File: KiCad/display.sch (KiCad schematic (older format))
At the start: 72 parts, among them IC11 SN74LV1T125DBVR, IC6 PCA9517ADP, J1 46756-1001, J2 2129320-3, T1 BSS138APW

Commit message: TLV70018DCKT -> TPS7A0518PDBVT
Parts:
- U? (x3): footprint jetson-nano-baseboard-footprints:TPD4E05U06QDQARQ1 -> antmicro-footprints:TPD4E05U06QDQARQ1; symbol jetson-nano-baseboard:TPD4E05U06QDQARQ1 -> antmicroTVSDiodes:TPD4E05U06QDQARQ1
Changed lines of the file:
@@
 Connection ~ 4025 4600
 $Comp
-L jetson-nano-baseboard:TPD4E05U06QDQARQ1 U?
+L antmicroTVSDiodes:TPD4E05U06QDQARQ1 U?
 U 1 1 61B4F31F
 P 14275 7150
 F 0 "U?" V 14301 7478 50  0000 L CNN
 F 1 "TPD4E05U06QDQARQ1" H 14325 6750 50  0001 L CNN
-F 2 "jetson-nano-baseboard-footprints:TPD4E05U06QDQARQ1" H 14325 7600 50  0001 L CNN
+F 2 "antmicro-footprints:TPD4E05U06QDQARQ1" H 14325 7600 50  0001 L CNN
 F 3 "http://www.ti.com/general/docs/lit/getliterature.tsp?genericPartNumber=TPD4E001&fileType=pdf" H 14275 7550 50  0001 L CNN
 F 4 "Texas Instruments" V 14650 6850 50  0000 L CNN "Manufacturer"
@@
 $EndComp
 $Comp
-L jetson-nano-baseboard:TPD4E05U06QDQARQ1 U?
+L antmicroTVSDiodes:TPD4E05U06QDQARQ1 U?
 U 1 1 61B58F0C
 P 13825 9275
 F 0 "U?" V 13900 9600 50  0000 L CNN
 F 1 "TPD4E05U06QDQARQ1" H 13875 8875 50  0001 L CNN
-F 2 "jetson-nano-baseboard-footprints:TPD4E05U06QDQARQ1" H 13875 9725 50  0001 L CNN
+F 2 "antmicro-footprints:TPD4E05U06QDQARQ1" H 13875 9725 50  0001 L CNN
 F 3 "http://www.ti.com/general/docs/lit/getliterature.tsp?genericPartNumber=TPD4E001&fileType=pdf" H 13825 9675 50  0001 L CNN
 F 4 "Texas Instruments" V 14200 8975 50  0000 L CNN "Manufacturer"
@@
 Connection ~ 10550 10025
 $Comp
-L jetson-nano-baseboard:TPD4E05U06QDQARQ1 U?
+L antmicroTVSDiodes:TPD4E05U06QDQARQ1 U?
 U 1 1 61E47ECC
 P 10650 10450
 F 0 "U?" V 10676 10778 50  0000 L CNN
 F 1 "TPD4E05U06QDQARQ1" H 10700 10050 50  0001 L CNN
-F 2 "jetson-nano-baseboard-footprints:TPD4E05U06QDQARQ1" H 10700 10900 50  0001 L CNN
+F 2 "antmicro-footprints:TPD4E05U06QDQARQ1" H 10700 10900 50  0001 L CNN
 F 3 "http://www.ti.com/general/docs/lit/getliterature.tsp?genericPartNumber=TPD4E001&fileType=pdf" H 10650 10850 50  0001 L CNN
 F 4 "Texas Instruments" V 11025 10150 50  0000 L CNN "Manufacturer"

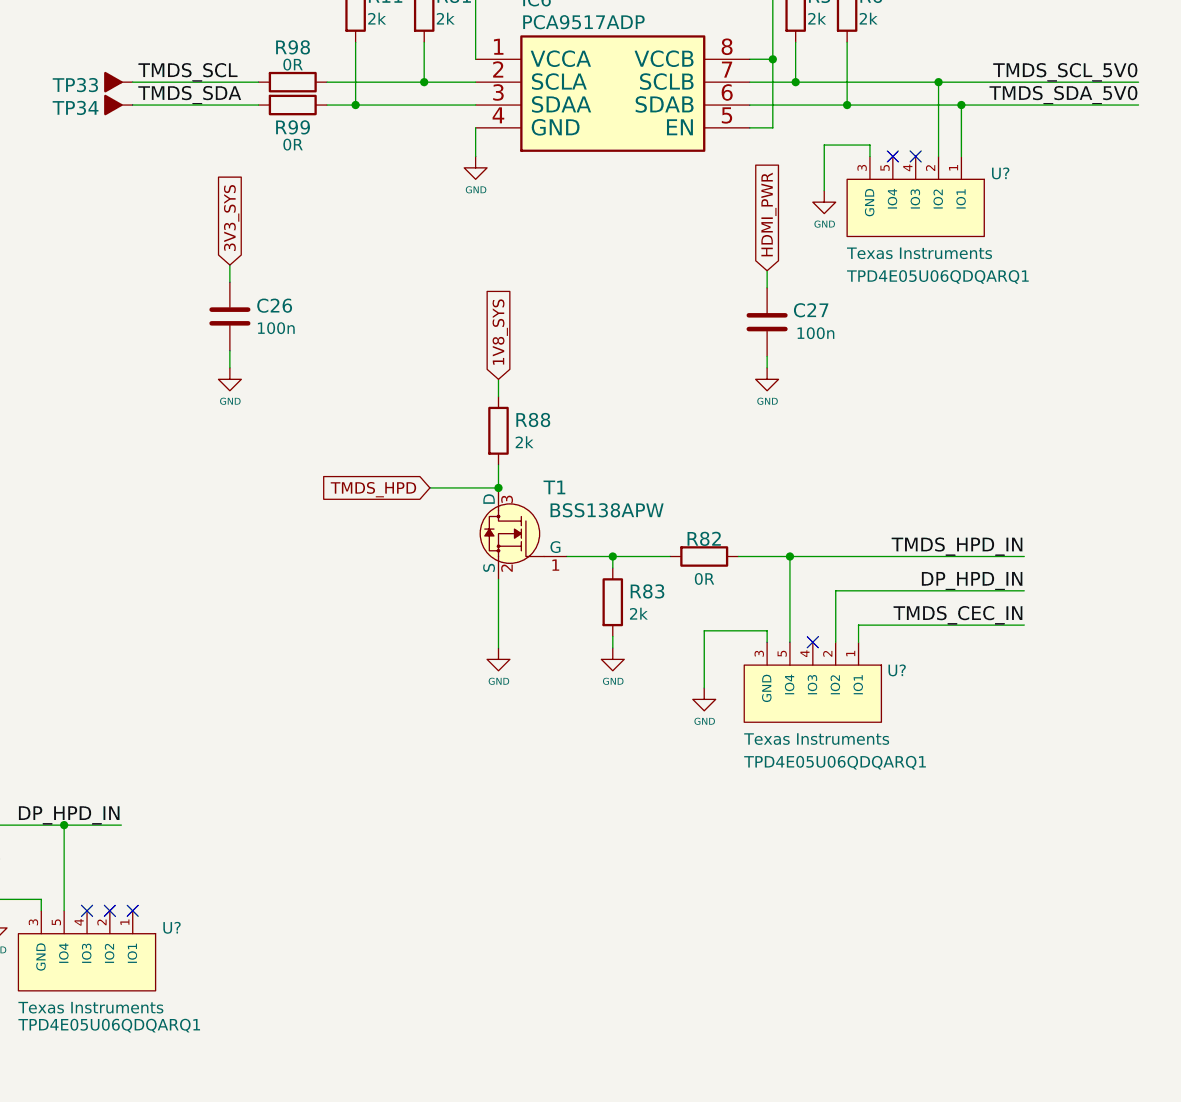
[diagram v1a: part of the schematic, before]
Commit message: Annotate parts
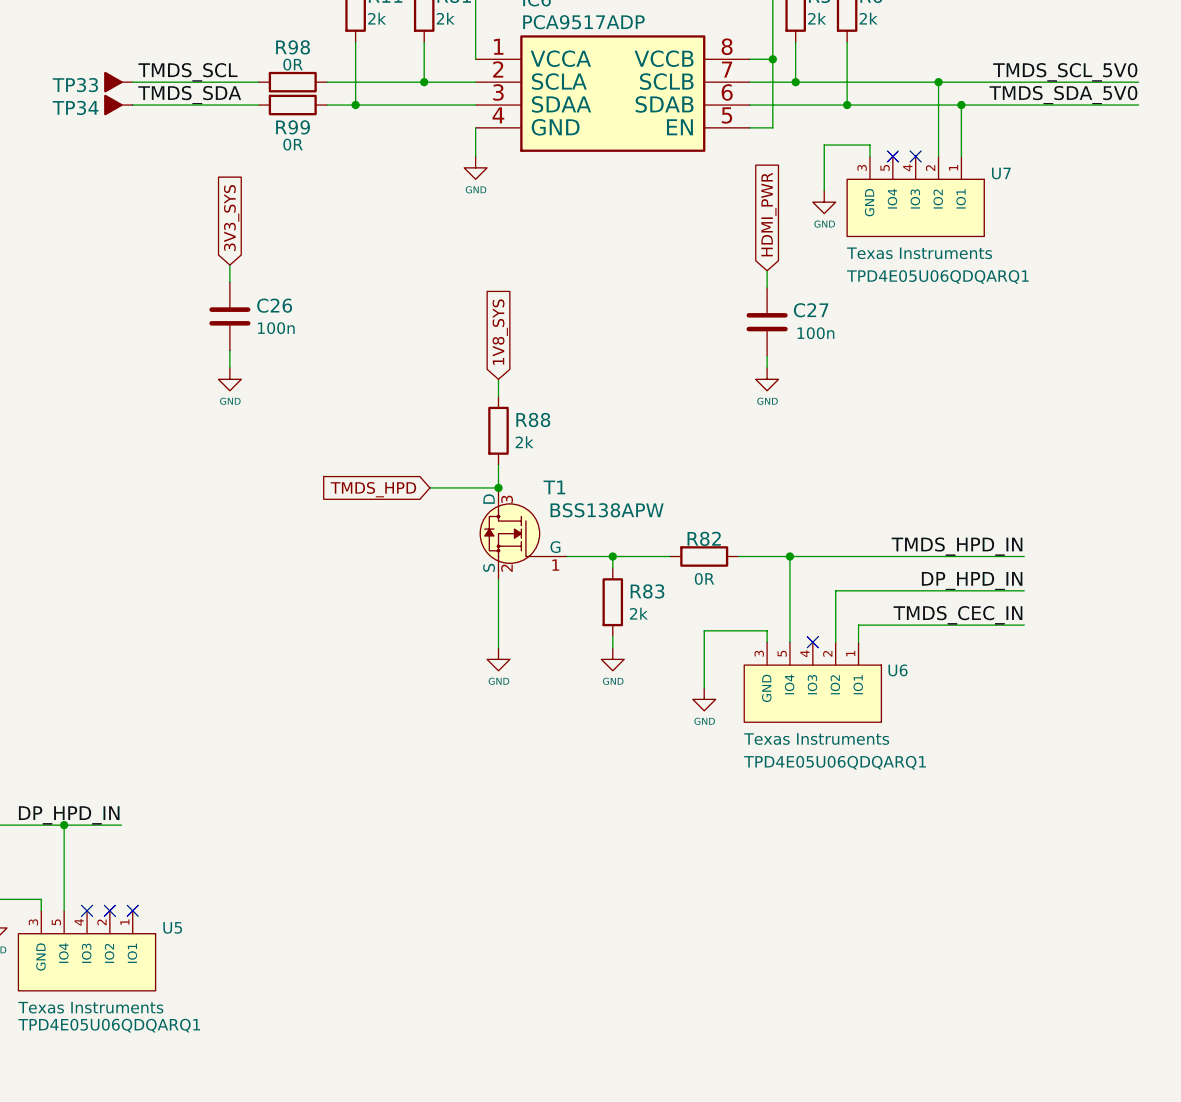
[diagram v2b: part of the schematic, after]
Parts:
- gave numbers to parts that had none: 3
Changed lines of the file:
@@
 Connection ~ 4025 4600
 $Comp
-L antmicroTVSDiodes:TPD4E05U06QDQARQ1 U?
+L antmicroTVSDiodes:TPD4E05U06QDQARQ1 U7
 U 1 1 61B4F31F
 P 14275 7150
-F 0 "U?" V 14301 7478 50  0000 L CNN
+F 0 "U7" V 14301 7478 50  0000 L CNN
 F 1 "TPD4E05U06QDQARQ1" H 14325 6750 50  0001 L CNN
 F 2 "antmicro-footprints:TPD4E05U06QDQARQ1" H 14325 7600 50  0001 L CNN
@@
 $EndComp
 $Comp
-L antmicroTVSDiodes:TPD4E05U06QDQARQ1 U?
+L antmicroTVSDiodes:TPD4E05U06QDQARQ1 U6
 U 1 1 61B58F0C
 P 13825 9275
-F 0 "U?" V 13900 9600 50  0000 L CNN
+F 0 "U6" V 13900 9600 50  0000 L CNN
 F 1 "TPD4E05U06QDQARQ1" H 13875 8875 50  0001 L CNN
 F 2 "antmicro-footprints:TPD4E05U06QDQARQ1" H 13875 9725 50  0001 L CNN
@@
 Connection ~ 10550 10025
 $Comp
-L antmicroTVSDiodes:TPD4E05U06QDQARQ1 U?
+L antmicroTVSDiodes:TPD4E05U06QDQARQ1 U5
 U 1 1 61E47ECC
 P 10650 10450
-F 0 "U?" V 10676 10778 50  0000 L CNN
+F 0 "U5" V 10676 10778 50  0000 L CNN
 F 1 "TPD4E05U06QDQARQ1" H 10700 10050 50  0001 L CNN
 F 2 "antmicro-footprints:TPD4E05U06QDQARQ1" H 10700 10900 50  0001 L CNN

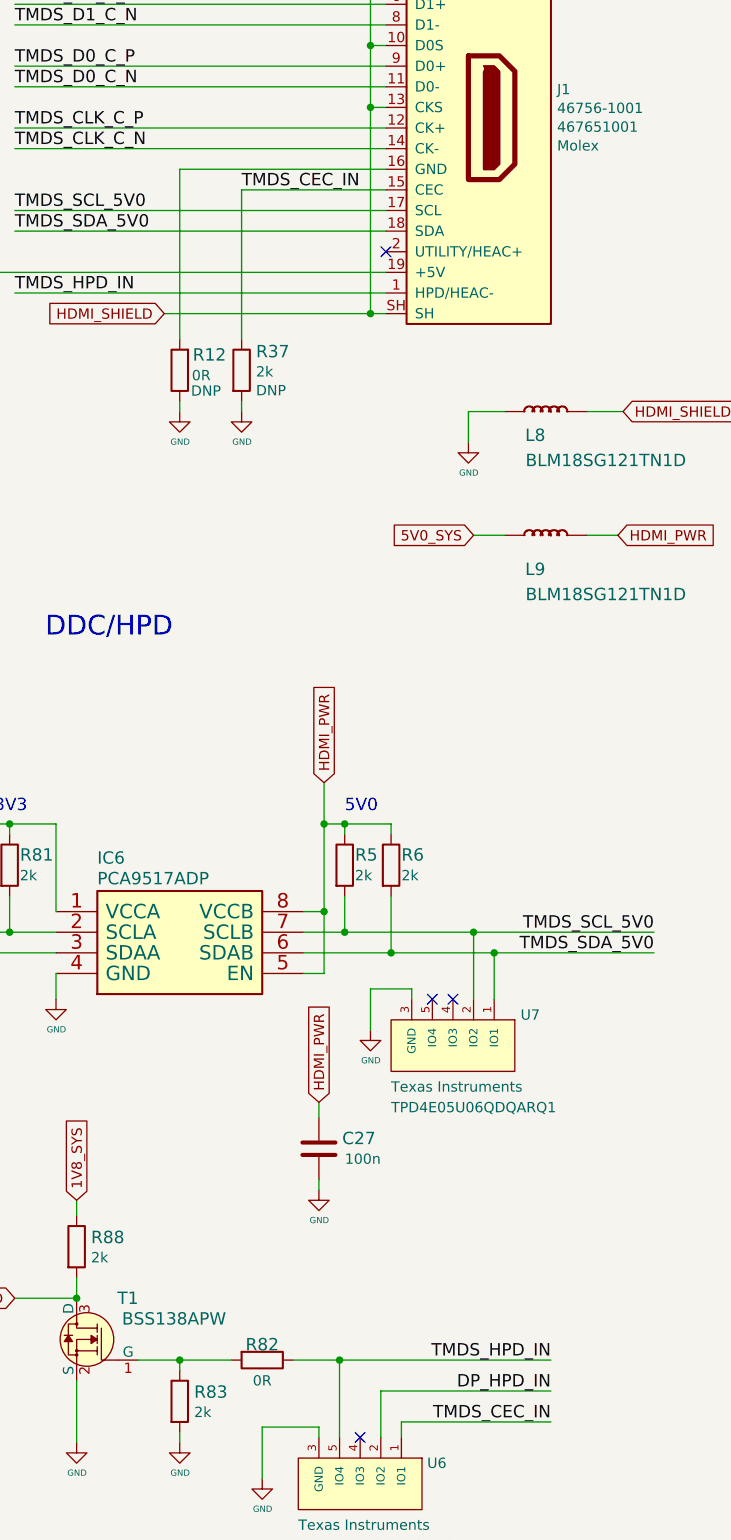
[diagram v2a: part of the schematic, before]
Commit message: Change connections to simplify routing
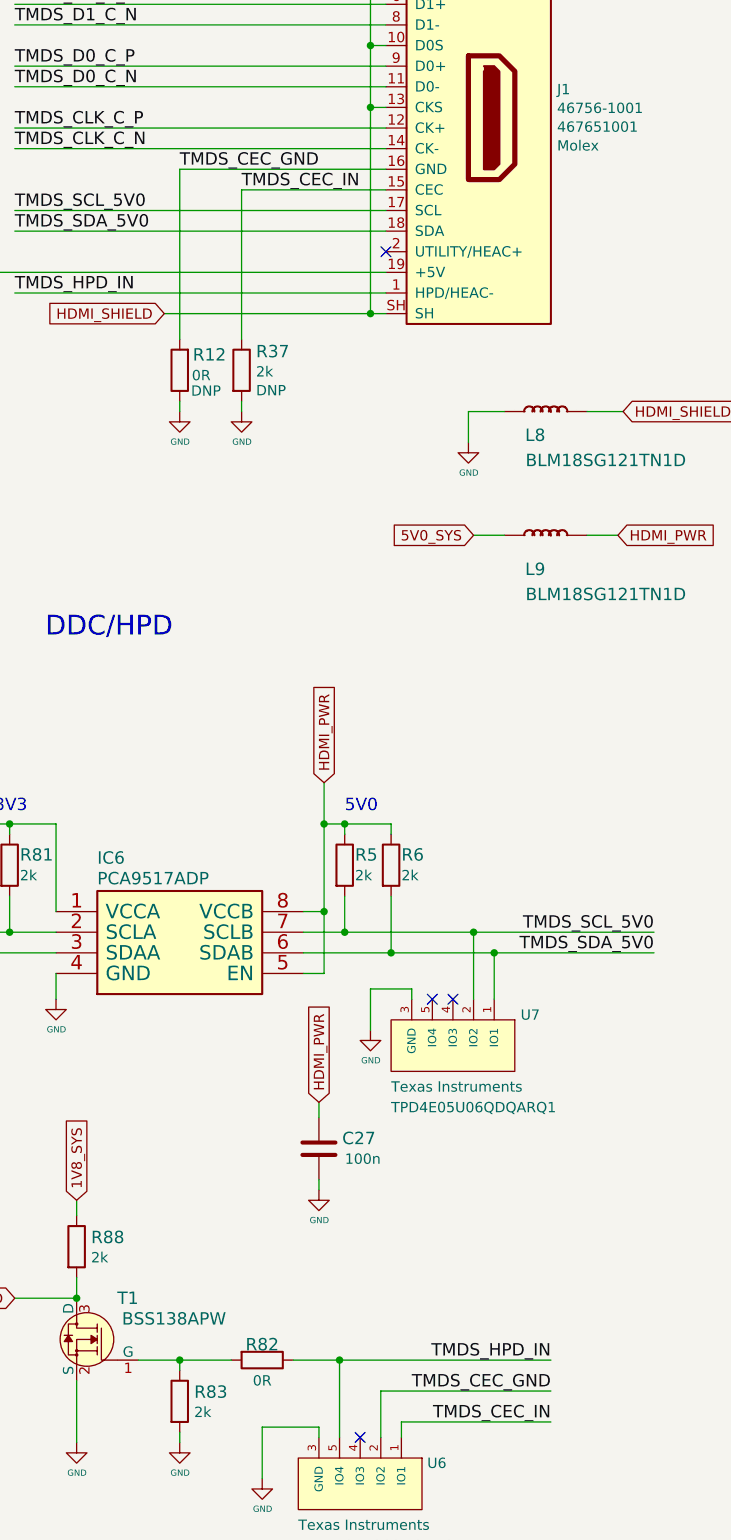
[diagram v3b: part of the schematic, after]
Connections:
- net DP_HPD_IN: no longer U6.2 (IO2), U6.9 (IO2)
- net TMDS_CEC_GND: now reaches J1.16 (GND), R12.2
- net TMDS_CEC_GND: now also U6.2 (IO2), U6.9 (IO2)
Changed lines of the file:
@@
 	13725 8850 14750 8850
 NoConn ~ 13825 9225
-Text Label 14750 9000 2    60   ~ 0
-DP_HPD_IN
 Wire Wire Line
 	14750 9000 13925 9000
@@
 NoConn ~ 10750 10400
 NoConn ~ 10850 10400
+Text Label 12950 3075 0    60   ~ 0
+TMDS_CEC_GND
+Text Label 14750 9000 2    60   ~ 0
+TMDS_CEC_GND
 $EndSCHEMATC

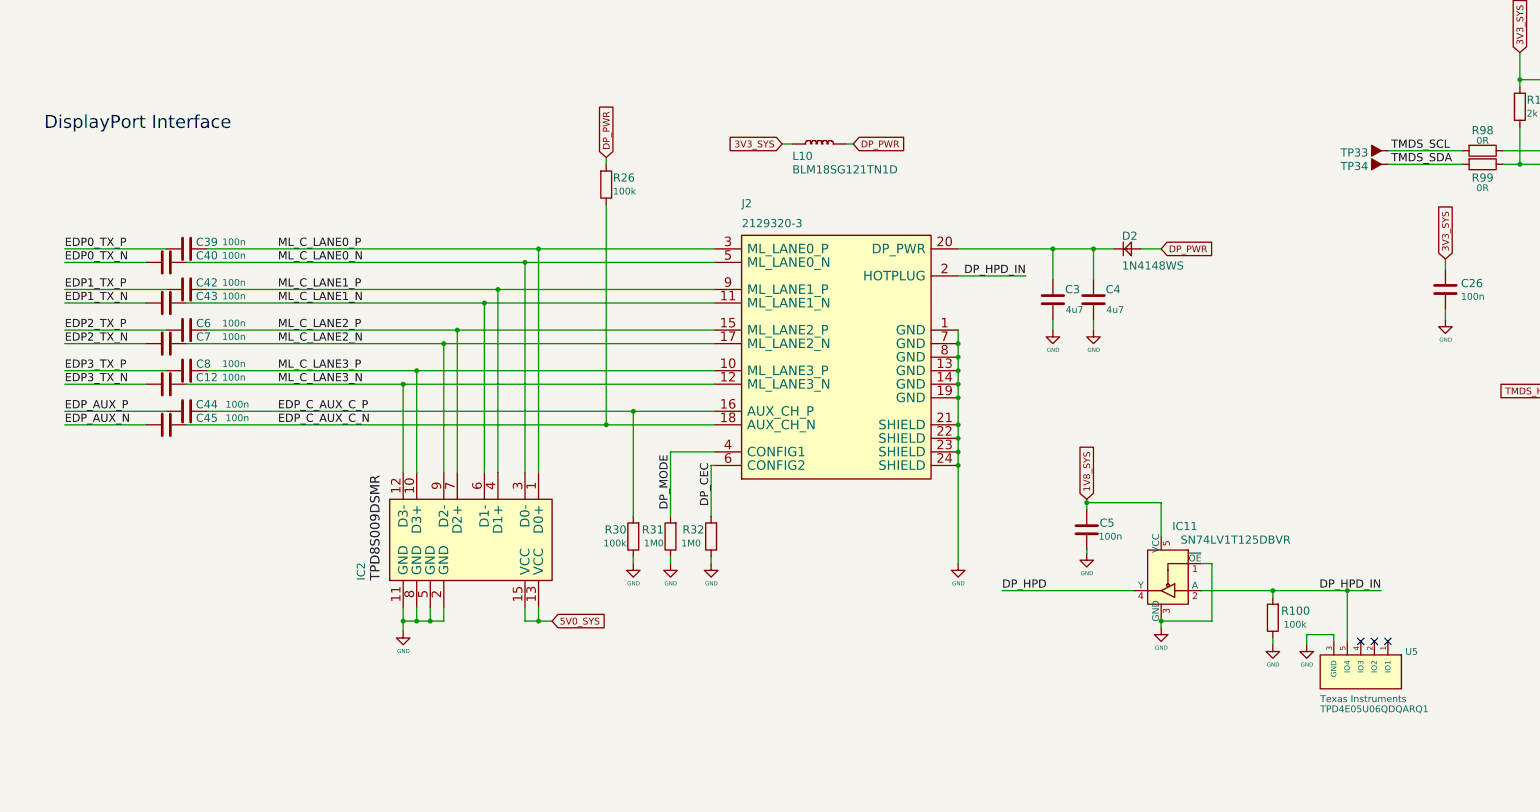
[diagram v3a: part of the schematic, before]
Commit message: Remove DP connector and TSVs
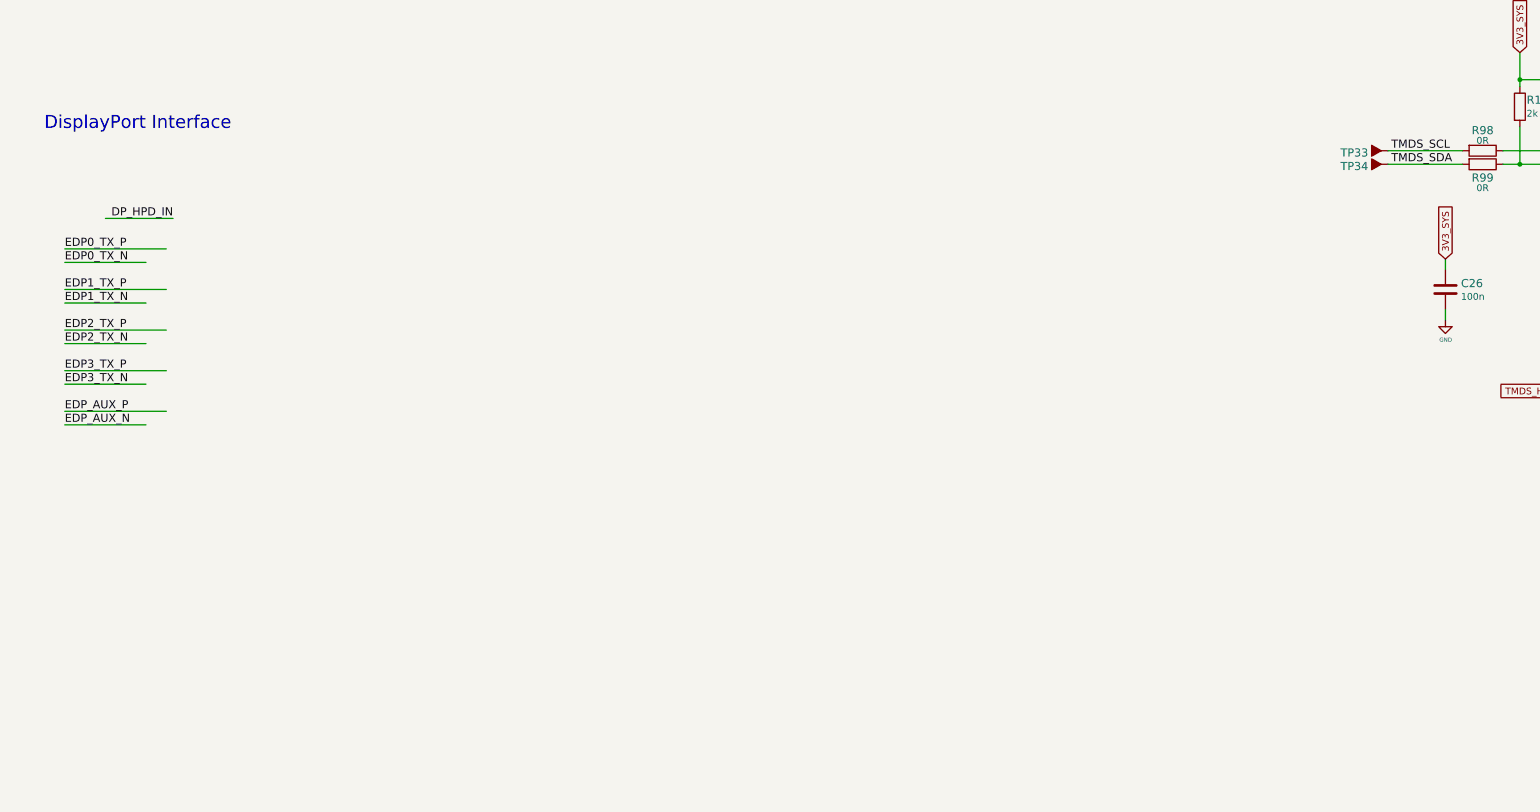
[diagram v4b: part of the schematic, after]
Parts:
- removed C12, C39, C40, C42, C43, C44, C45, C5, C6, C7, C8: C_100n_0402, jetson-nano-baseboard-footprints:0402-cap, symbol jetson-nano-baseboard:C_100n_0402
- removed C3, C4: C_4u7_0402, jetson-nano-baseboard-footprints:0402-cap, symbol jetson-nano-baseboard:C_4u7_0402
- removed D2: 1N4148WS, jetson-nano-baseboard-footprints:SOD-323, symbol jetson-nano-baseboard:diode
- removed IC11: SN74LV1T125DBVR, jetson-nano-baseboard-footprints:SOT-23-5, symbol jetson-nano-baseboard:SN74LV1T125DBVR
- removed IC2: ~, jetson-nano-baseboard-footprints:SON-15, symbol jetson-nano-baseboard:TPD8S009
- removed J2: 2129320-3, jetson-nano-baseboard-footprints:2129320-3, symbol jetson-nano-baseboard:miniDP
- removed L10: BLM18SG121TN1D, jetson-nano-baseboard-footprints:0603, symbol jetson-nano-baseboard:BLM18SG121TN1D
- removed R100, R26, R30: R_100k_0402, jetson-nano-baseboard-footprints:0402-res, symbol jetson-nano-baseboard:R_100k_0402
- removed R31, R32: R_1M0_0402, jetson-nano-baseboard-footprints:0402-res, symbol jetson-nano-baseboard:R_1M0_0402
- removed U5: TPD4E05U06QDQARQ1, antmicro-footprints:TPD4E05U06QDQARQ1, symbol antmicroTVSDiodes:TPD4E05U06QDQARQ1
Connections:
- net labels removed: DP_CEC, DP_MODE, DP_PWR, EDP_C_AUX_C_N, EDP_C_AUX_C_P, ML_C_LANE0_N, ML_C_LANE0_P, ML_C_LANE1_N, ML_C_LANE1_P, ML_C_LANE2_N, ML_C_LANE2_P, ML_C_LANE3_N, ML_C_LANE3_P
- wire segments 281 -> 191
- no-connect marks 8 -> 5
